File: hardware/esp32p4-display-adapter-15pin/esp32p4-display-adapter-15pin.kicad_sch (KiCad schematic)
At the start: 6 parts, among them J1 ESP32-P4_DSI_15pin, J2 Display_30pin, J3 GPIO_Header, U1 AP2127K-2.8, U2 AP2127K-1.8, U3 TXB0102

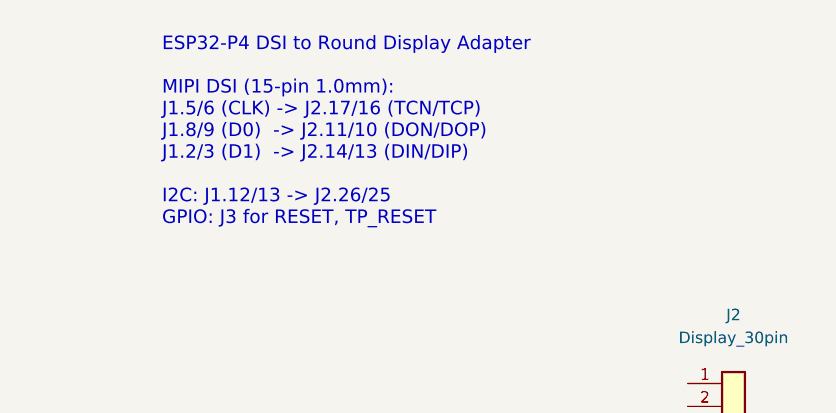
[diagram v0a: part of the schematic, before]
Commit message: Restore esp32p4-display-adapter (22-pin), add esp32p4-display-adapter-15pin
- esp32p4-display-adapter: 22-pin 0.5mm (your working version restored)
- esp32p4-display-adapter-15pin: NEW - 15-pin 1.0mm (same pinout as RPi)
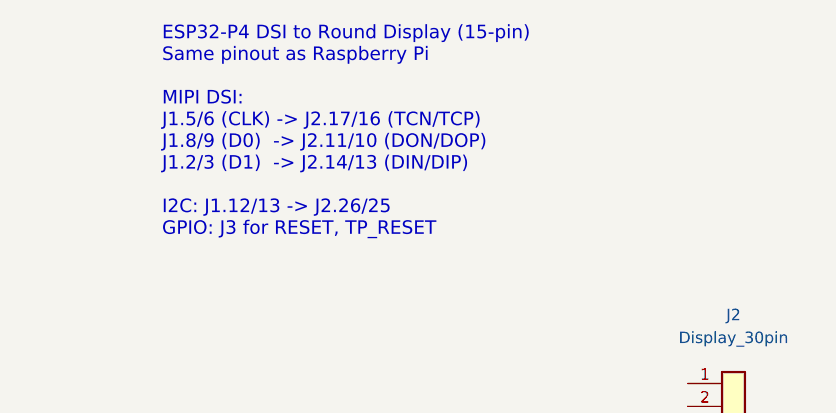
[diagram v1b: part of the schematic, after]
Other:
- note added: "ESP32-P4 DSI to Round Display (15-pin) Same pinout as Raspberry Pi MIPI DSI: J1.5/6 (CLK) -> J2.17/16 (TCN/TCP) J1.8/9 (D0) -> J2.11/10 (DON/DOP) J1.2/3 (D1) -> J2.14/13 (DIN/DIP) I2C: J1.12/13 -> J2.26/25 GPIO: J3 for RESET, TP_RESET"
- note removed: "ESP32-P4 DSI to Round Display Adapter MIPI DSI (15-pin 1.0mm): J1.5/6 (CLK) -> J2.17/16 (TCN/TCP) J1.8/9 (D0) -> J2.11/10 (DON/DOP) J1.2/3 (D1) -> J2.14/13 (DIN/DIP) I2C: J1.12/13 -> J2.26/25 GPIO: J3 for RESET, TP_RESET"
- title: ESP32-P4 DSI to Round Display Adapter -> ESP32-P4 DSI to Round Display Adapter (15-pin)
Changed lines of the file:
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@@
   (paper "A4")
   (title_block
-    (title "ESP32-P4 DSI to Round Display Adapter")
+    (title "ESP32-P4 DSI to Round Display Adapter (15-pin)")
     (date "2026-04-24")
-    (rev "1.1")
+    (rev "1.0")
     (company "bimmerz.app / OpenCluster")
   )
@@
     (pin "15")
     (instances
-      (project "esp32p4-display-adapter"
-        (path "/a1b2c3d4-e5f6-7890-abcd-ef1234567890" (reference "J1") (unit 1))
+      (project "esp32p4-display-adapter-15pin"
+        (path "/d4e5f6a7-b8c9-0123-def4-567890123456" (reference "J1") (unit 1))
       )
     )
@@
     (pin "30")
     (instances
-      (project "esp32p4-display-adapter"
-        (path "/a1b2c3d4-e5f6-7890-abcd-ef1234567890" (reference "J2") (unit 1))
+      (project "esp32p4-display-adapter-15pin"
+        (path "/d4e5f6a7-b8c9-0123-def4-567890123456" (reference "J2") (unit 1))
       )
     )
@@
     (pin "4")
     (instances
-      (project "esp32p4-display-adapter"
-        (path "/a1b2c3d4-e5f6-7890-abcd-ef1234567890" (reference "J3") (unit 1))
+      (project "esp32p4-display-adapter-15pin"
+        (path "/d4e5f6a7-b8c9-0123-def4-567890123456" (reference "J3") (unit 1))
       )
     )
@@
     (pin "5")
     (instances
-      (project "esp32p4-display-adapter"
-        (path "/a1b2c3d4-e5f6-7890-abcd-ef1234567890" (reference "U1") (unit 1))
+      (project "esp32p4-display-adapter-15pin"
+        (path "/d4e5f6a7-b8c9-0123-def4-567890123456" (reference "U1") (unit 1))
       )
     )
@@
     (pin "5")
     (instances
-      (project "esp32p4-display-adapter"
-        (path "/a1b2c3d4-e5f6-7890-abcd-ef1234567890" (reference "U2") (unit 1))
+      (project "esp32p4-display-adapter-15pin"
+        (path "/d4e5f6a7-b8c9-0123-def4-567890123456" (reference "U2") (unit 1))
       )
     )
@@
     (pin "8")
     (instances
-      (project "esp32p4-display-adapter"
-        (path "/a1b2c3d4-e5f6-7890-abcd-ef1234567890" (reference "U3") (unit 1))
+      (project "esp32p4-display-adapter-15pin"
+        (path "/d4e5f6a7-b8c9-0123-def4-567890123456" (reference "U3") (unit 1))
       )
     )
   )
-  (text "ESP32-P4 DSI to Round Display Adapter\n\nMIPI DSI (15-pin 1.0mm):\nJ1.5/6 (CLK) -> J2.17/16 (TCN/TCP)\nJ1.8/9 (D0)  -> J2.11/10 (DON/DOP)\nJ1.2/3 (D1)  -> J2.14/13 (DIN/DIP)\n\nI2C: J1.12/13 -> J2.26/25\nGPIO: J3 for RESET, TP_RESET"
+  (text "ESP32-P4 DSI to Round Display (15-pin)\nSame pinout as Raspberry Pi\n\nMIPI DSI:\nJ1.5/6 (CLK) -> J2.17/16 (TCN/TCP)\nJ1.8/9 (D0)  -> J2.11/10 (DON/DOP)\nJ1.2/3 (D1)  -> J2.14/13 (DIN/DIP)\n\nI2C: J1.12/13 -> J2.26/25\nGPIO: J3 for RESET, TP_RESET"
     (exclude_from_sim no)
     (at 88.9 25.4 0)
